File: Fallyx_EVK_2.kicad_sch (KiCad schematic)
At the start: 6 parts, among them J1 Conn_01x05_Pin, U2 ILPS22QSTR

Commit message: review edits
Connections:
- net V_IN is gone; now on net 1V8: J1.1 (Pin_1)

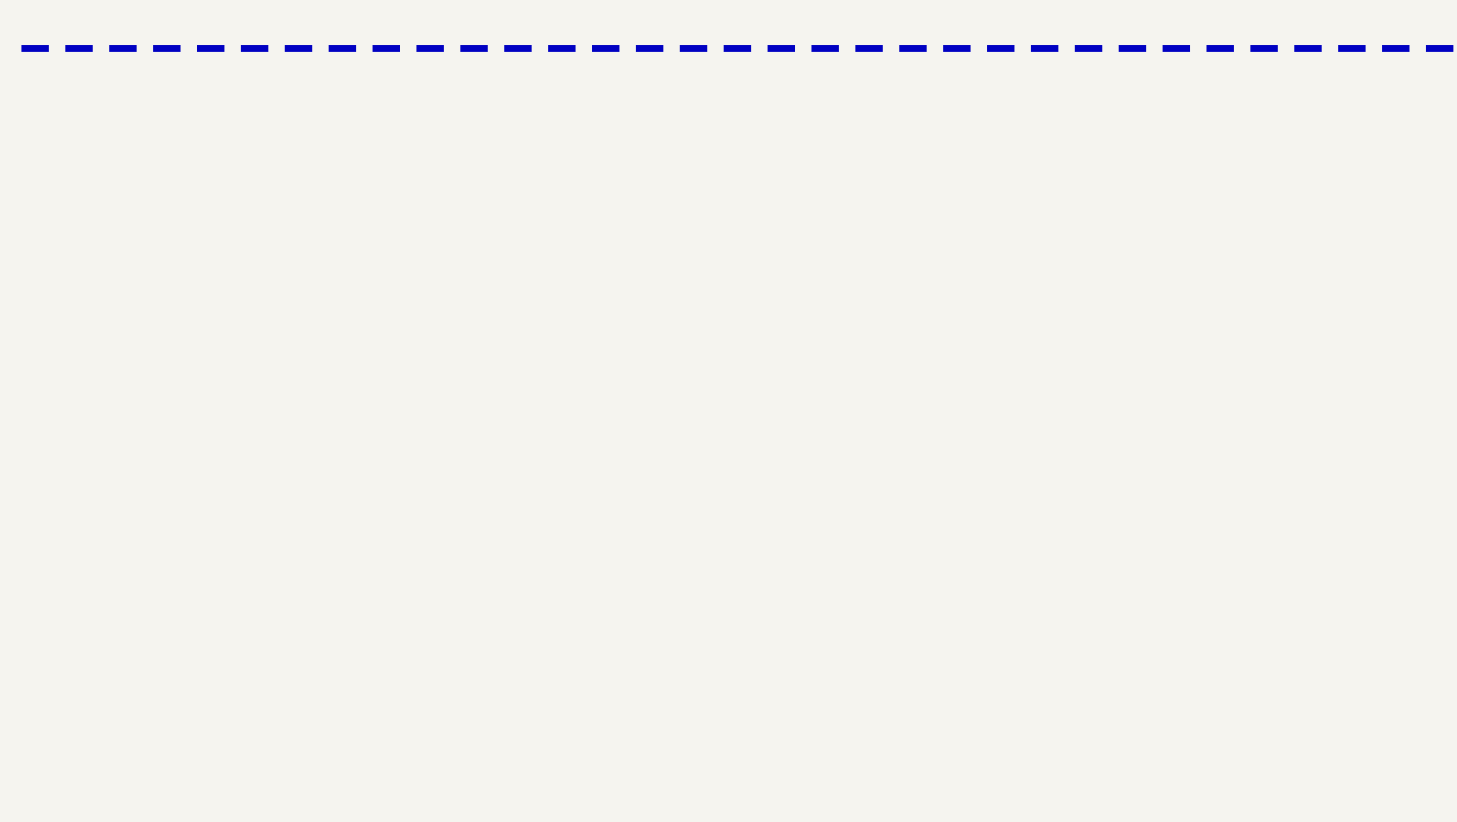
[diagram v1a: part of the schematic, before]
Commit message: Updated for new BLE modules
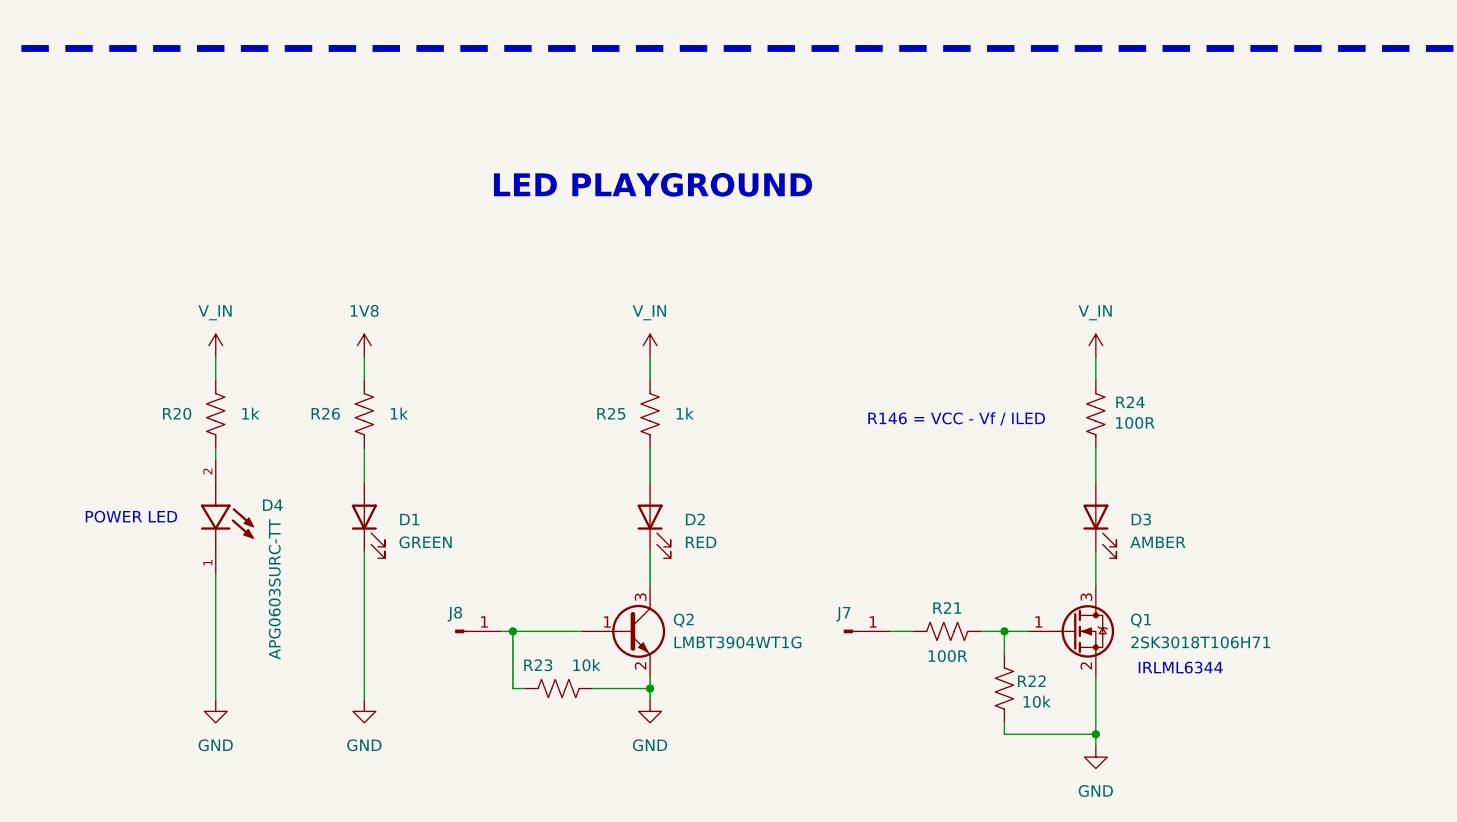
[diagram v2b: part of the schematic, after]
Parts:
- added D1: GREEN, LED_SMD:LED_0603_1608Metric, symbol Device:LED
- added D2: RED, LED_SMD:LED_0603_1608Metric, symbol Device:LED
- added D3: AMBER, LED_SMD:LED_0603_1608Metric, symbol Device:LED
- added D4: APG0603SURC-TT, APG0603SURC-TT:LED_APG0603SURC-TT, symbol APG0603SURC-TT:APG0603SURC-TT
- added J7, J8: Conn_01x01_Pin, Connector_PinHeader_2.54mm:PinHeader_1x01_P2.54mm_Vertical, symbol Connector:Conn_01x01_Pin
- added Q1: 2SK3018T106H71, Package_TO_SOT_SMD:SOT-323_SC-70, symbol Transistor_FET:IRLML0030
- added Q2: LMBT3904WT1G, Package_TO_SOT_SMD:SOT-23, symbol Transistor_BJT:SS8050
- added R20, R25, R26: 1k, Resistor_SMD:R_0402_1005Metric, symbol Device:R_US
- added R21, R24: 100R, Resistor_SMD:R_0402_1005Metric, symbol Device:R_US
- added R22, R23: 10k, Resistor_SMD:R_0402_1005Metric, symbol Device:R_US
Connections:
- net 1V8: now also R26.1
- net GND: now also D1.1 (K), D4.1, Q1.2 (S), Q2.2 (E), R22.2, R23.1
- new net: Q1.1 (G), R21.1, R22.1
- new net: D3.1 (K), Q1.3 (D)
- new net: J7.1 (Pin_1), R21.2
- new net: D3.2 (A), R24.2
- new net: J8.1 (Pin_1), Q2.1 (B), R23.2
- new net: D1.2 (A), R26.2
- new net: D2.1 (K), Q2.3 (C)
- new net: D2.2 (A), R25.2
- new net: D4.2, R20.2
- new net V_IN: R20.1, R24.1, R25.1
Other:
- note added: "IRLML6344"
- note added: "LED PLAYGROUND"
- note added: "POWER LED"
- note added: "R146 = VCC - Vf / ILED"
